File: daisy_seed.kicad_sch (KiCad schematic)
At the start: 21 parts, among them J2 GPIO Header, J3 Micro_SD_Card, U3 Daisy_Seed, U4 H11L1SM

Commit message: dealing with protection circuit changes
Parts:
- renumbered D2 to D3
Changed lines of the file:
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@@
 		(dnp no)
 		(fields_autoplaced yes)
-		(property "Reference" "#PWR014"
+		(property "Reference" "#PWR017"
 			(at 74.93 238.76 0)
 			(effects
@@
 			(project "triptech"
 				(path "/55cca6a8-30da-4c13-b2f2-a01401e2b54c/75aee282-6ddd-4543-b5fc-0fc86bf548ec"
-					(reference "#PWR014")
+					(reference "#PWR017")
 					(unit 1)
 				)
@@
 		(dnp no)
 		(fields_autoplaced yes)
-		(property "Reference" "#PWR021"
+		(property "Reference" "#PWR024"
 			(at 260.35 124.46 0)
 			(effects
@@
 			(project "triptech"
 				(path "/55cca6a8-30da-4c13-b2f2-a01401e2b54c/75aee282-6ddd-4543-b5fc-0fc86bf548ec"
-					(reference "#PWR021")
+					(reference "#PWR024")
 					(unit 1)
 				)
@@
 		(dnp no)
 		(fields_autoplaced yes)
-		(property "Reference" "#PWR019"
+		(property "Reference" "#PWR022"
 			(at 237.49 88.9 0)
 			(effects
@@
 			(project ""
 				(path "/55cca6a8-30da-4c13-b2f2-a01401e2b54c/75aee282-6ddd-4543-b5fc-0fc86bf548ec"
-					(reference "#PWR019")
+					(reference "#PWR022")
 					(unit 1)
 				)
@@
 		(dnp no)
 		(fields_autoplaced yes)
-		(property "Reference" "#PWR016"
+		(property "Reference" "#PWR019"
 			(at 78.74 152.4 0)
 			(effects
@@
 			(project ""
 				(path "/55cca6a8-30da-4c13-b2f2-a01401e2b54c/75aee282-6ddd-4543-b5fc-0fc86bf548ec"
-					(reference "#PWR016")
+					(reference "#PWR019")
 					(unit 1)
 				)
@@
 		(dnp no)
 		(fields_autoplaced yes)
-		(property "Reference" "#PWR015"
+		(property "Reference" "#PWR018"
 			(at 78.74 68.58 0)
 			(effects
@@
 			(project ""
 				(path "/55cca6a8-30da-4c13-b2f2-a01401e2b54c/75aee282-6ddd-4543-b5fc-0fc86bf548ec"
-					(reference "#PWR015")
+					(reference "#PWR018")
 					(unit 1)
 				)
@@
 		(dnp no)
 		(fields_autoplaced yes)
-		(property "Reference" "#PWR023"
+		(property "Reference" "#PWR026"
 			(at 341.63 151.13 0)
 			(effects
@@
 			(project "triptech"
 				(path "/55cca6a8-30da-4c13-b2f2-a01401e2b54c/75aee282-6ddd-4543-b5fc-0fc86bf548ec"
-					(reference "#PWR023")
+					(reference "#PWR026")
 					(unit 1)
 				)
@@
 		(dnp no)
 		(fields_autoplaced yes)
-		(property "Reference" "#PWR022"
+		(property "Reference" "#PWR025"
 			(at 260.35 149.86 0)
 			(effects
@@
 			(project "triptech"
 				(path "/55cca6a8-30da-4c13-b2f2-a01401e2b54c/75aee282-6ddd-4543-b5fc-0fc86bf548ec"
-					(reference "#PWR022")
+					(reference "#PWR025")
 					(unit 1)
 				)
@@
 		(dnp no)
 		(fields_autoplaced yes)
-		(property "Reference" "#PWR018"
+		(property "Reference" "#PWR021"
 			(at 181.61 181.61 0)
 			(effects
@@
 			(project ""
 				(path "/55cca6a8-30da-4c13-b2f2-a01401e2b54c/75aee282-6ddd-4543-b5fc-0fc86bf548ec"
-					(reference "#PWR018")
+					(reference "#PWR021")
 					(unit 1)
 				)
@@
 		(dnp no)
 		(fields_autoplaced yes)
-		(property "Reference" "#PWR017"
+		(property "Reference" "#PWR020"
 			(at 86.36 68.58 0)
 			(effects
@@
 			(project ""
 				(path "/55cca6a8-30da-4c13-b2f2-a01401e2b54c/75aee282-6ddd-4543-b5fc-0fc86bf548ec"
-					(reference "#PWR017")
+					(reference "#PWR020")
 					(unit 1)
 				)
@@
 		(dnp no)
 		(fields_autoplaced yes)
-		(property "Reference" "D2"
+		(property "Reference" "D3"
 			(at 274.32 102.8699 90)
 			(effects
@@
 			(project ""
 				(path "/55cca6a8-30da-4c13-b2f2-a01401e2b54c/75aee282-6ddd-4543-b5fc-0fc86bf548ec"
-					(reference "D2")
+					(reference "D3")
 					(unit 1)
 				)
@@
 		(dnp no)
 		(fields_autoplaced yes)
-		(property "Reference" "#PWR013"
+		(property "Reference" "#PWR016"
 			(at 71.12 68.58 0)
 			(effects
@@
 			(project ""
 				(path "/55cca6a8-30da-4c13-b2f2-a01401e2b54c/75aee282-6ddd-4543-b5fc-0fc86bf548ec"
-					(reference "#PWR013")
+					(reference "#PWR016")
 					(unit 1)
 				)
@@
 		(dnp no)
 		(fields_autoplaced yes)
-		(property "Reference" "#PWR020"
+		(property "Reference" "#PWR023"
 			(at 245.11 259.08 0)
 			(effects
@@
 			(project "triptech"
 				(path "/55cca6a8-30da-4c13-b2f2-a01401e2b54c/75aee282-6ddd-4543-b5fc-0fc86bf548ec"
-					(reference "#PWR020")
-					(unit 1)
-				)
+					(reference "#PWR023")
+					(unit 1)
+				)

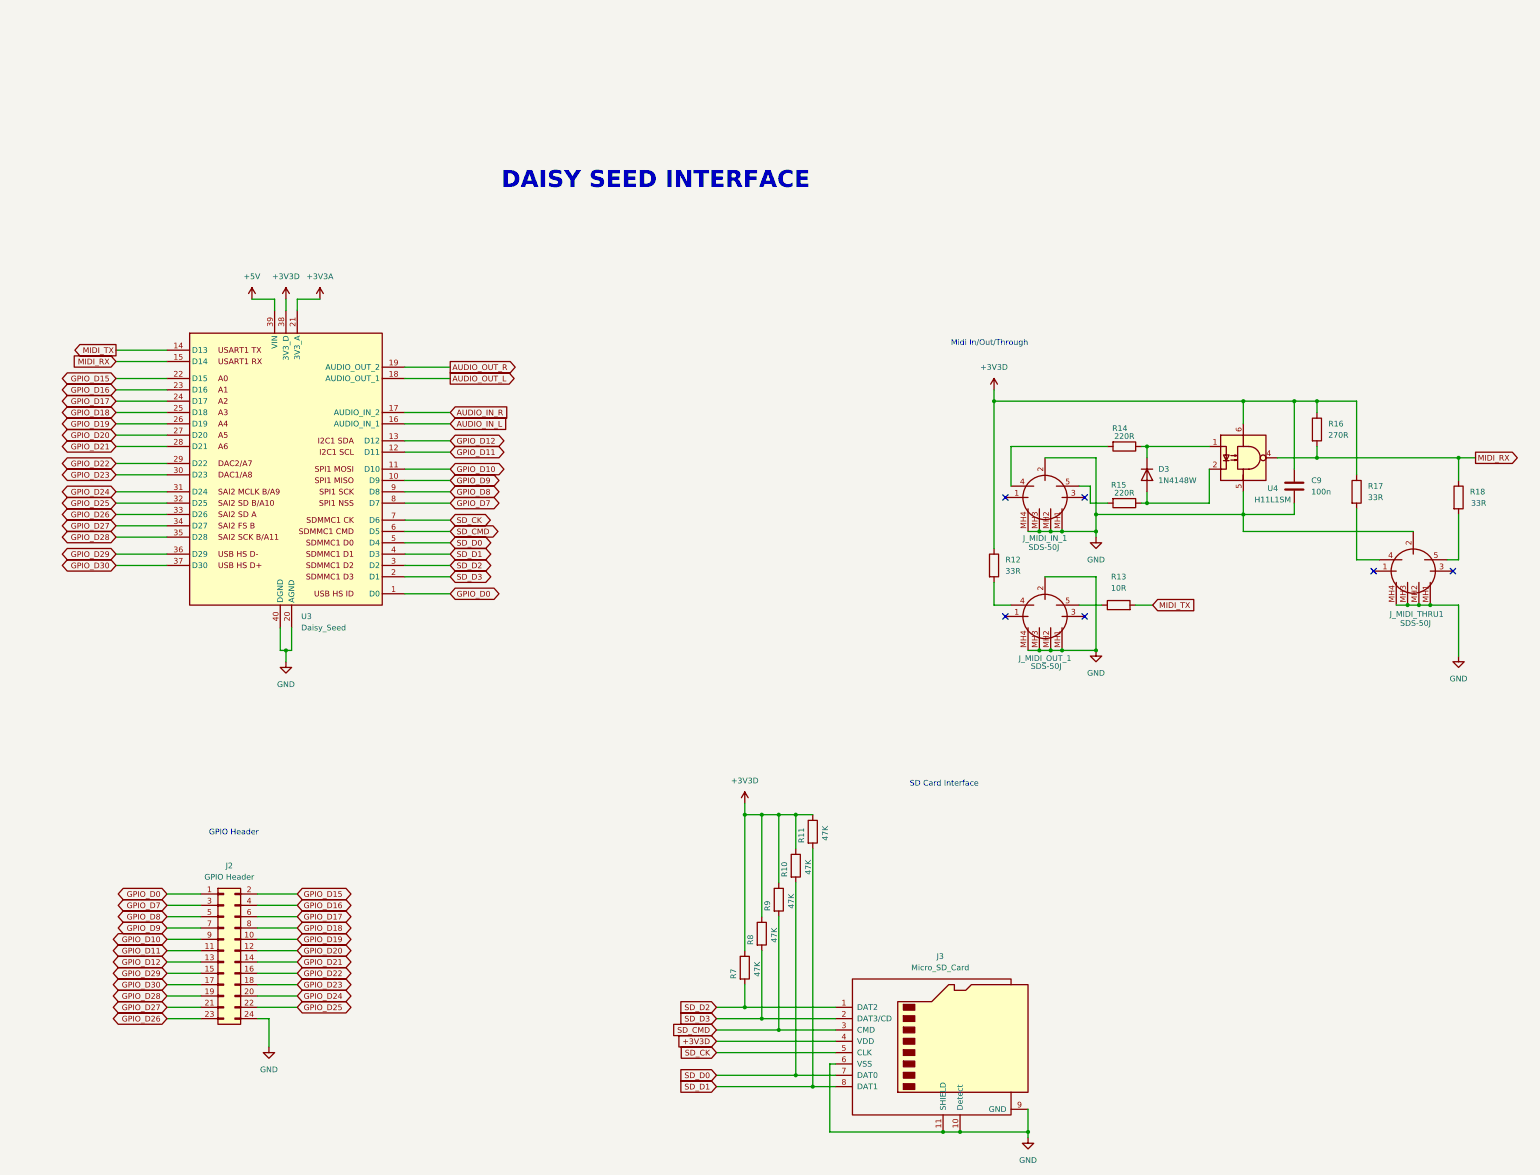
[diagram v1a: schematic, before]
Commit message: audio input for rev 2 laid out in schematic
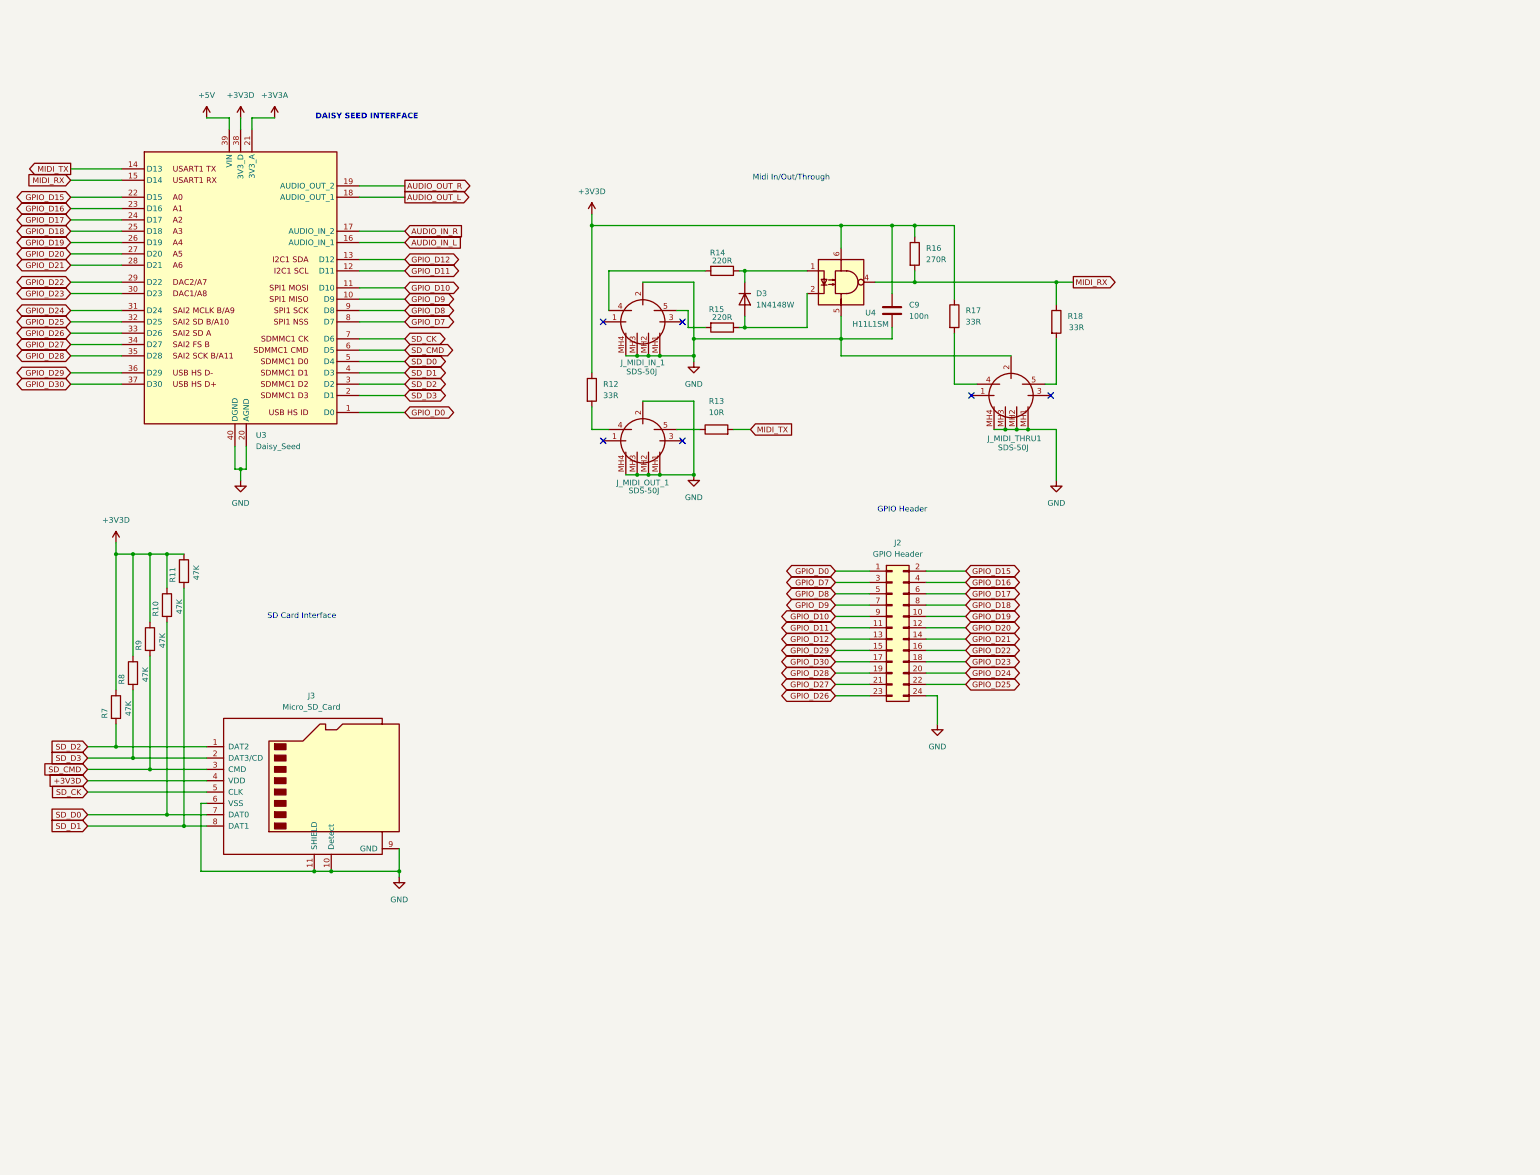
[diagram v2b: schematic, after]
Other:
- company: (none) -> Rasheed Abdul-Aziz
- title: Triptech - Daisy Seed Interface -> Daisy-Studio
- moved on the sheet: C9, D3, J2, J3, J_MIDI_IN_1, J_MIDI_OUT_1, J_MIDI_THRU1, R10, R11, R12, R13, R14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

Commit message: output design update
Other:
- note added: "Todo: C_AA (anti alias from input section)"
- note added: "Todo: Use Best routing to update the pin assignments."
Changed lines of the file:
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@@
+		)
+	)
+	(text "Todo: C_AA (anti alias from input section)"
+		(exclude_from_sim no)
+		(at 123.952 51.308 90)
+		(effects
+			(font
+				(size 2.54 2.54)
+				(color 255 26 37 1)
+			)
+		)
+	)
+	(text "Todo: Use Best routing to update the pin assignments."
+		(exclude_from_sim no)
+		(at 216.662 136.398 0)
+		(effects
+			(font
+				(size 2.54 2.54)
+				(color 255 26 37 1)
+			)
 		)
 	)

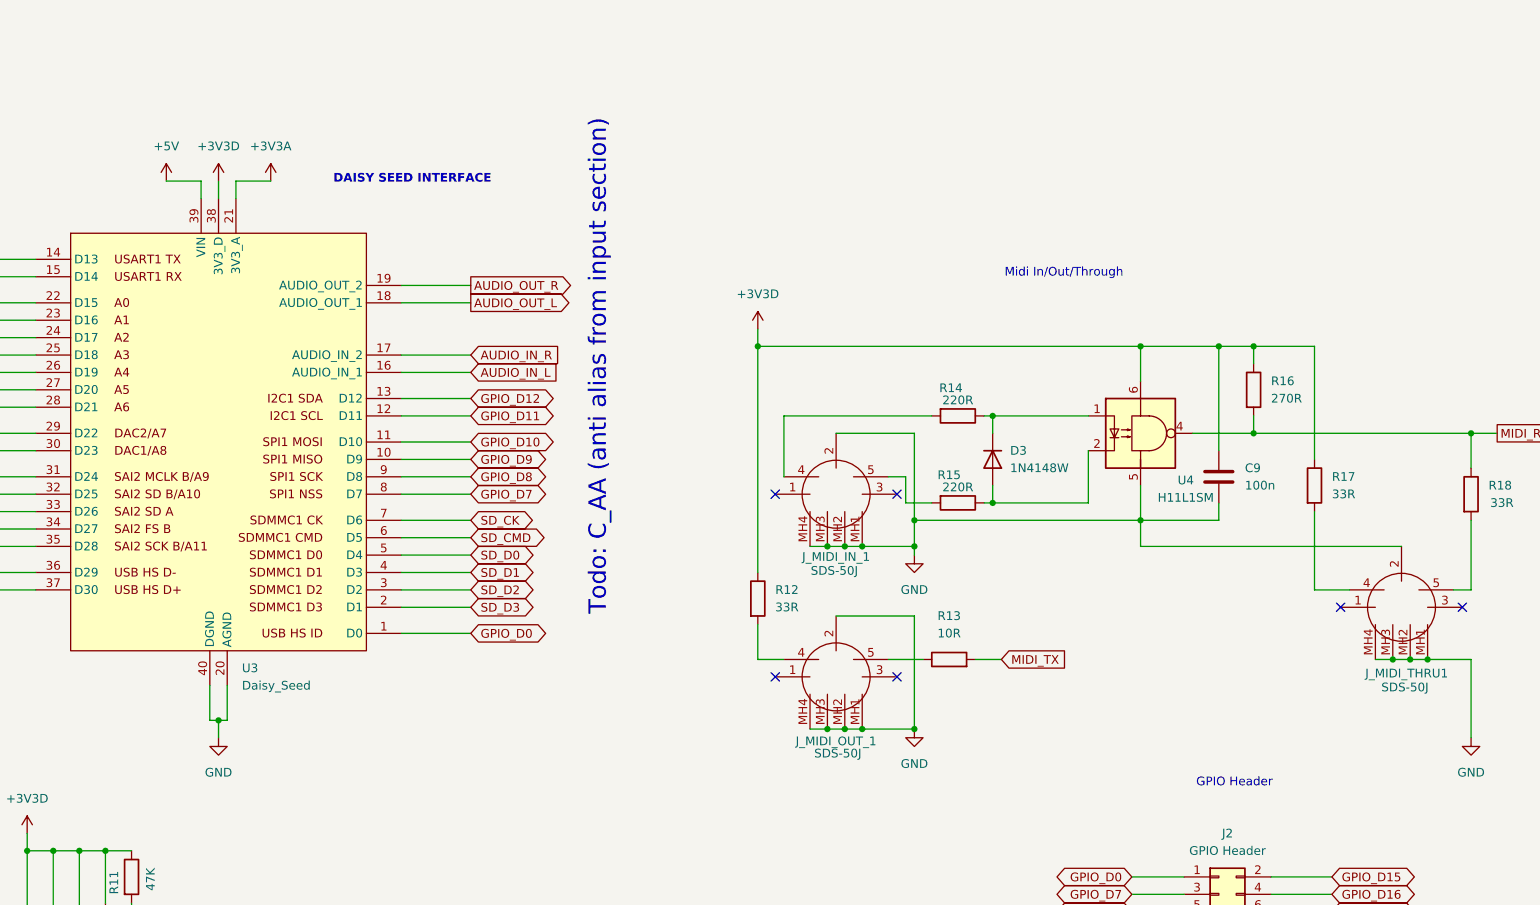
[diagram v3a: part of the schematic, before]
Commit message: Cleanup and review of input pt 1
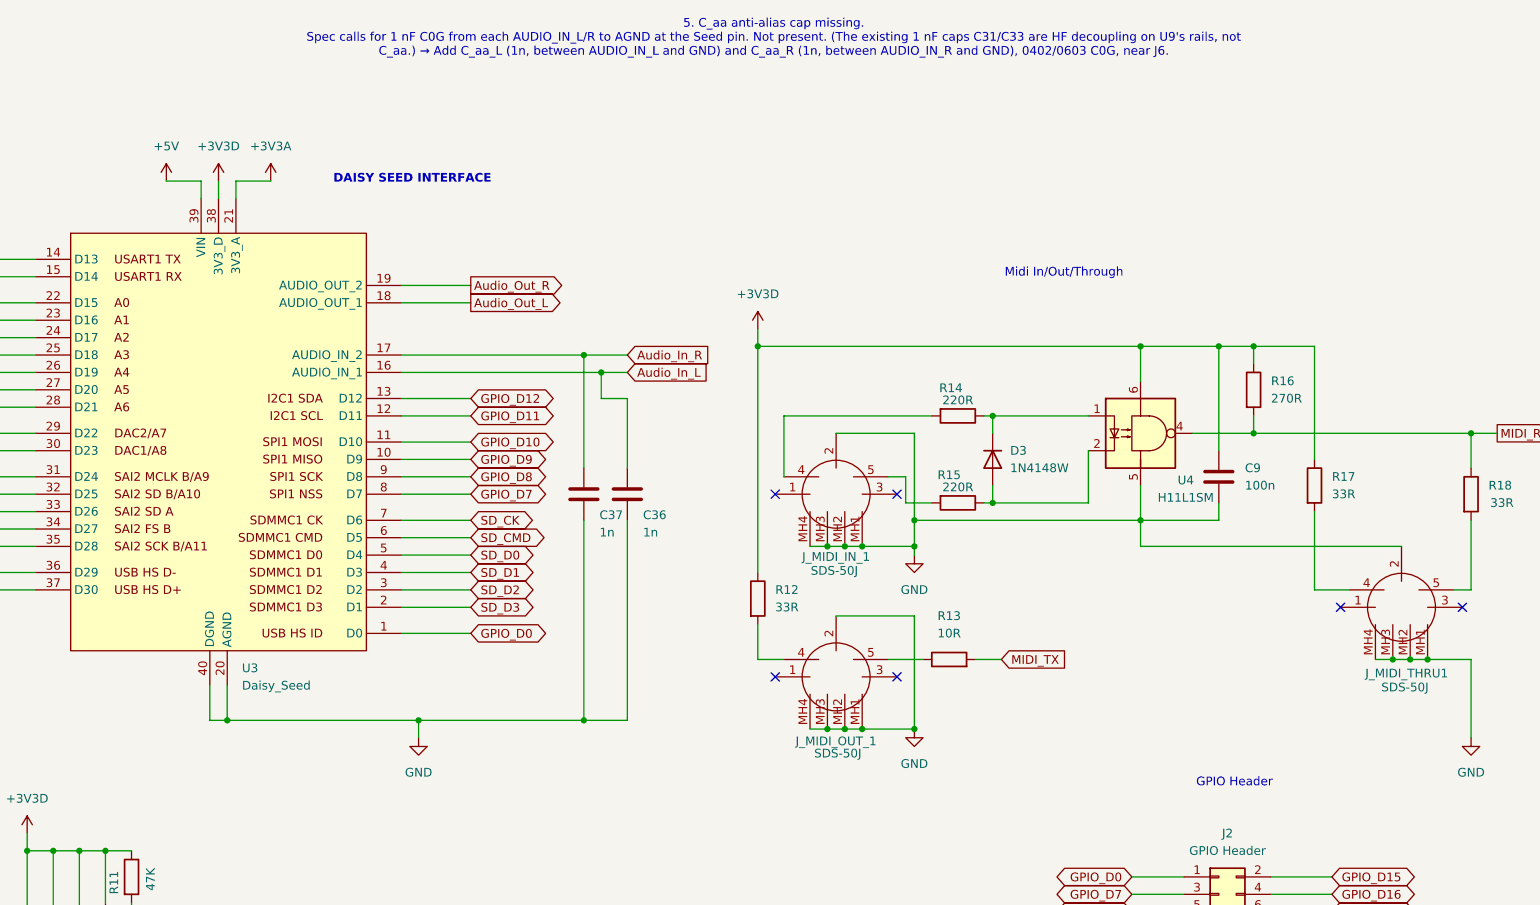
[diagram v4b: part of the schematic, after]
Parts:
- added C36, C37: 1n, Capacitor_SMD:C_0603_1608Metric, symbol Device:C
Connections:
- net GND: now also C36.2, C37.2
- net AUDIO_IN_L renamed Audio_In_L
- net Audio_In_L: now also C36.1
- net AUDIO_IN_R renamed Audio_In_R
- net Audio_In_R: now also C37.1
- net AUDIO_OUT_L renamed Audio_Out_L
- net AUDIO_OUT_R renamed Audio_Out_R
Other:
- note added: "5. C_aa anti-alias cap missing. Spec calls for 1 nF C0G from each AUDIO_IN_L/R to AGND at the Seed pin. Not present. (The existing 1 nF caps C31/C33 are HF decoupling on U9's rails, not C_aa.) → Add C_aa_L (1n, between AUDIO_IN_L and GND) and C_aa_R (1n, between AUDIO_IN_R and GND), 0402/0603 C0G, near J6."
- note removed: "Todo: C_AA (anti alias from input section)"
